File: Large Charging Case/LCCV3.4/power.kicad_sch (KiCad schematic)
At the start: 43 parts, among them J23 USB_C_Receptacle_USB2.0, J24 Conn_01x03, U16 ETA9882, U22 ME6215

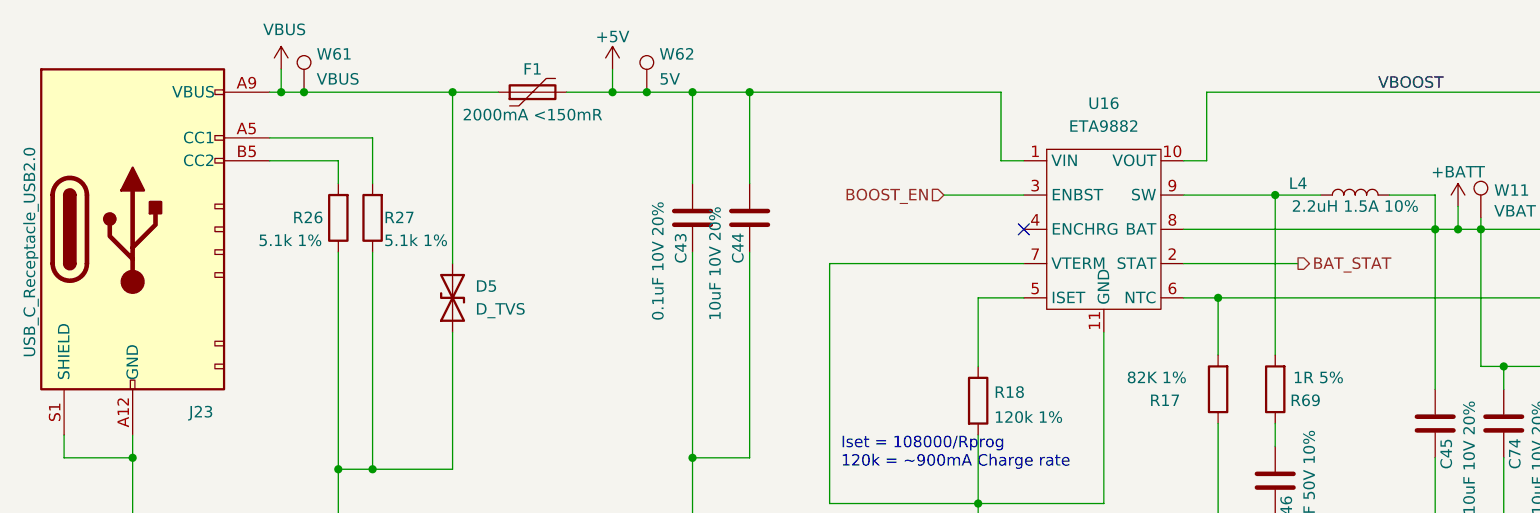
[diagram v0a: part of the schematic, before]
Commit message: Updated all boards based on Wang Qing's feedback. Generated renders of all boards. Updated LCC to Kicad 7.
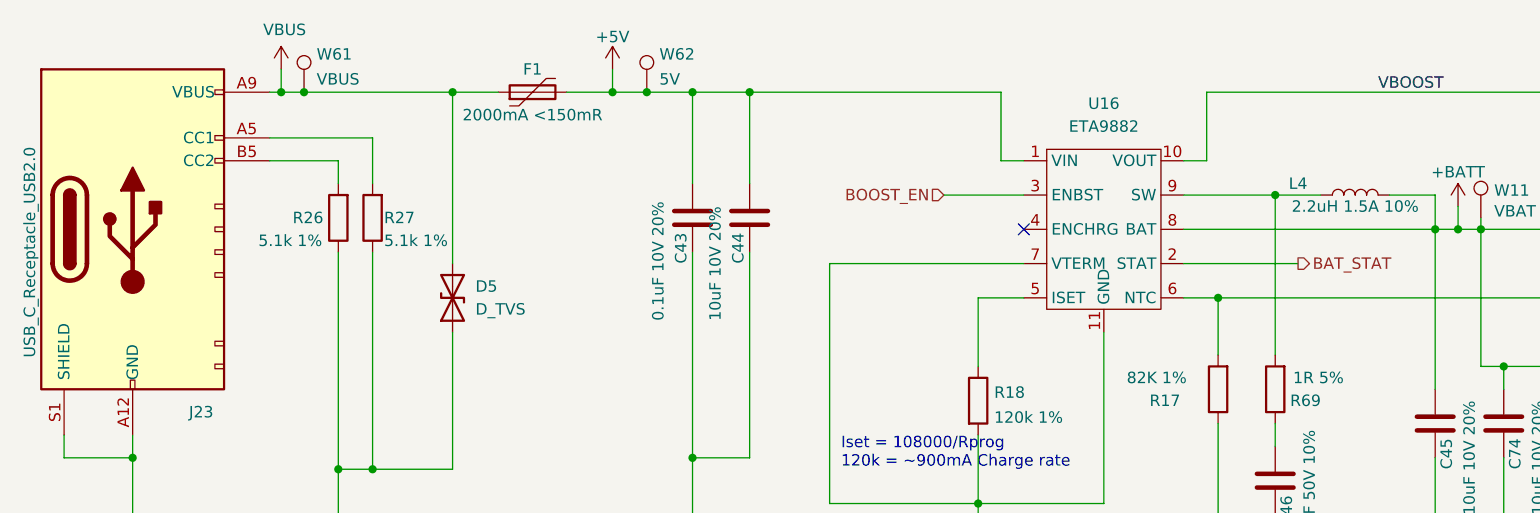
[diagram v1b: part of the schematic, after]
